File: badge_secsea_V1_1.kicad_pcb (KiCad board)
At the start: 4 copper layers, 74.1 x 130 mm, 132 parts, among them J1 USB_C_Receptacle_USB2.0_14P, J4 AFC07-S24ECA-00, J5 Micro_SD_Card_Det1, Q1 2N7002, Q2 SI1308EDL, Q3 SI2301, SW1 TS-1187A-B-A-B, SW2 K2-1112SW-A4SW-04, SW3 K2-1112SW-A4SW-04, SW4 XDTD-6650, SW5 XDTD-6650, SW6 TS-1187A-B-A-B, SW7 SW_SPDT, U1 RP2040, U2 74HC139, U3 W25Q128JVSIQ, U4 CC1101RGPR, U5 TP4056, U6 TPS63000, U7 LM321, X1 ABM8-272-T3, X2 26MHz

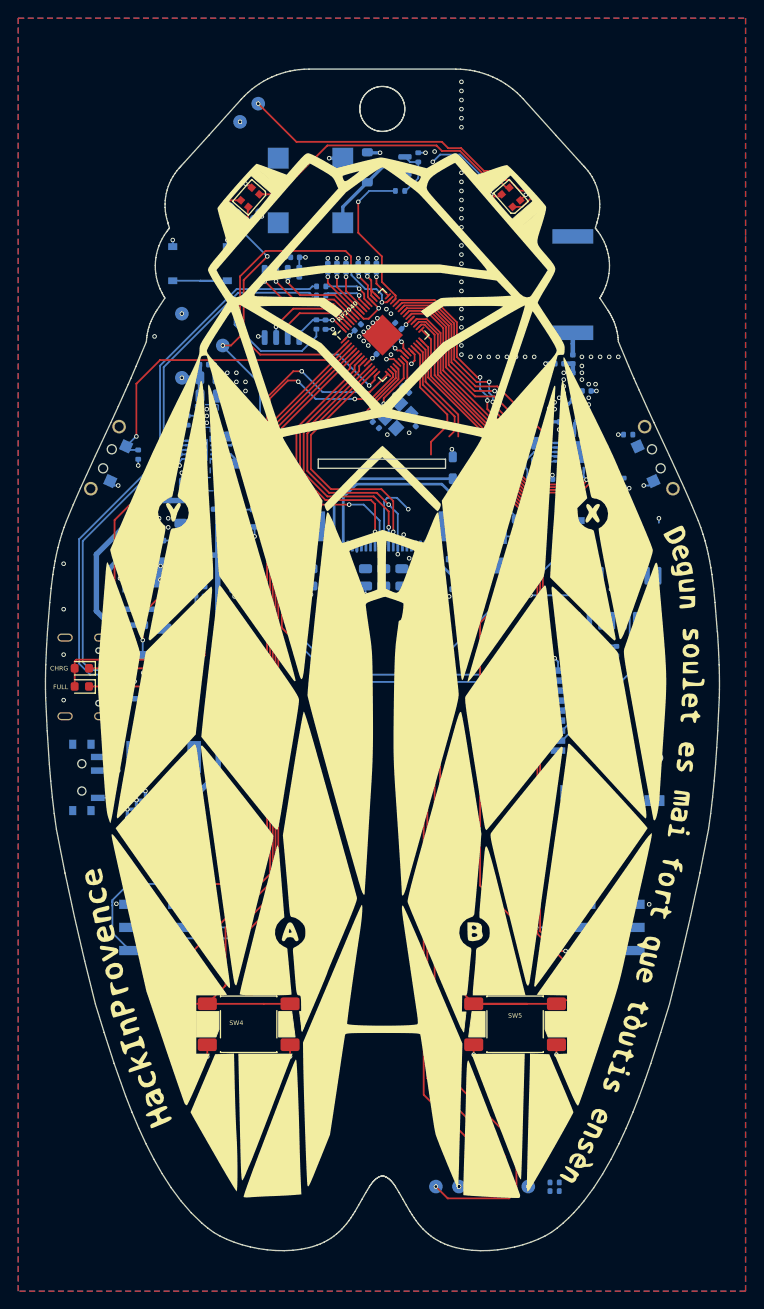
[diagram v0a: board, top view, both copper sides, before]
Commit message: fix: complete PCB routing with clean DRC
All tracks are routed. DRC passes with no errors. Remaining warnings are related to silkscreen graphics and footprint libraries, likely due to outdated footprints following KiCad updates.
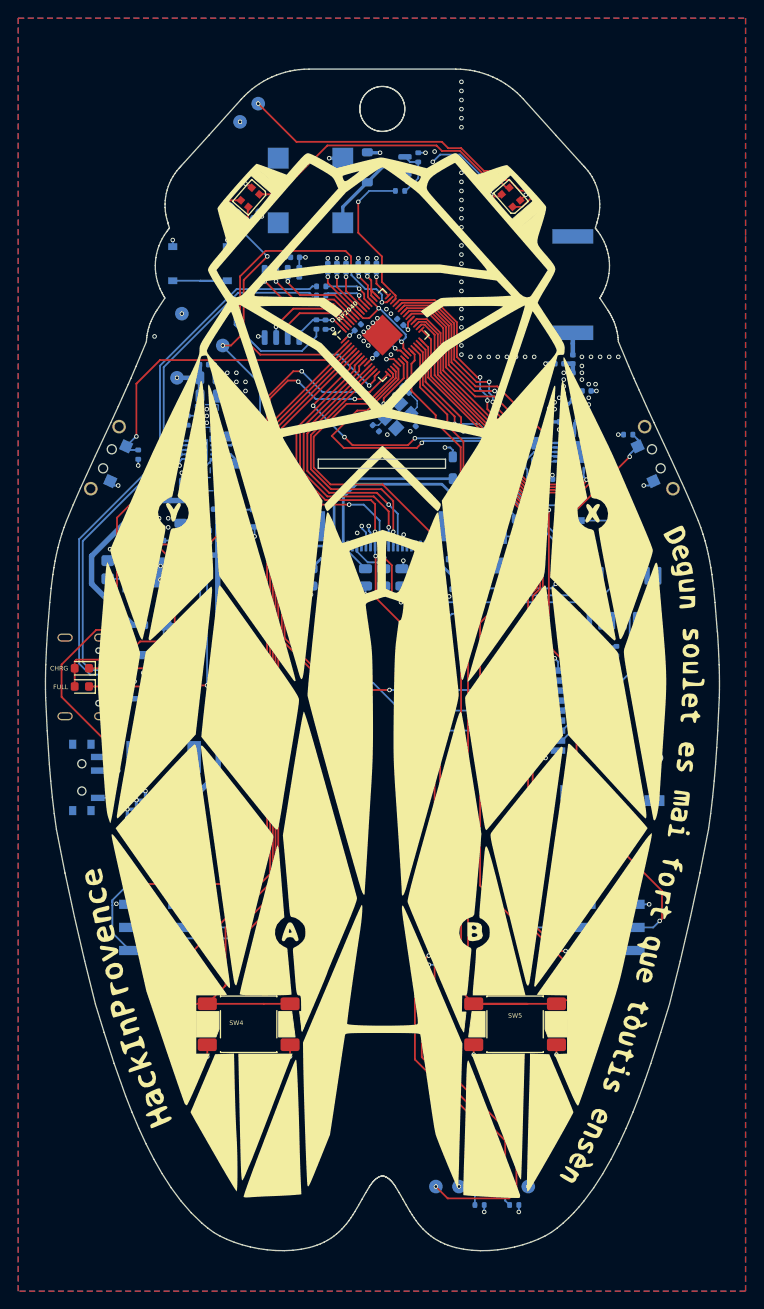
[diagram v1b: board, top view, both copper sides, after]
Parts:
- moved R21 15.1 mm to (69.8, 90.7), turned to -90 degrees
- moved R23 8.62 mm to (110.7, 160.5)
- moved R7 7.52 mm to (120.4, 85.3)
- moved R22 4.70 mm to (114.6, 160.5)
- moved R27 2.81 mm to (79.5, 90.4), turned to 0 degrees
- moved R19 1.61 mm to (79.5, 91.4), turned to 0 degrees
- moved R31 1.23 mm to (71.6, 96.8)
- moved C44 1.13 mm to (118.0, 110.2)
- moved R26 0.79 mm to (80.5, 86.4), turned to 180 degrees
- moved TP9 0.53 mm to (77.5, 69.5)
- moved C4 0.48 mm to (102.0, 63.4)
- moved C37 0.42 mm to (78.2, 97.7)
- moved R20 0.36 mm to (76.0, 98.2)
- moved C10 0.36 mm to (99.3, 75.1)
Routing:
- net I2C0_SDA: track 12.1 -> 80.0 mm, vias 0 -> 3
- net GPIO15_BUTTON_X: track 6.43 -> 59.6 mm, vias 0 -> 3
- net SPI0_CSn: track 4.02 -> 48.0 mm, vias 2 -> 3
- net GPIO14_BUTTON_B: track 66.2 -> 103.5 mm, vias 2 -> 1
- net SPI0_TX_MOSI: track 41.5 -> 78.6 mm, vias 1 -> 3
- net Net-(U1-SWCLK): track 67.2 -> 103.7 mm
- net RUN: track 106.7 -> 136.3 mm, vias 2 -> 7
- net Net-(U1-SWD): track 80.0 -> 104.5 mm, vias 2 -> 3
- net SPI0_CS0_SCREEN: track 9.83 -> 32.2 mm
- net Net-(SW7-B): track 28.7 -> 48.0 mm
- net +3.3V: track 80.0 -> 92.9 mm, vias 52 -> 55
- net Net-(U7-+): track 3.20 -> 12.5 mm, vias 2 -> 4
- net Net-(D7-K): track 20.7 -> 26.6 mm
- net SCREEN_RESE: track 0.00 -> 5.89 mm
- net Net-(U1-VREG_VOUT): track 16.4 -> 21.5 mm
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
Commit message: fix: update footprints to clear most DRC library warnings
Updated footprints to resolve the majority of DRC warnings. Remaining warnings: silkscreen issues and missing "Partek" footprint library are still unresolved.
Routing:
- net GND: track 88.4 -> 89.3 mm, vias 188 -> 189
